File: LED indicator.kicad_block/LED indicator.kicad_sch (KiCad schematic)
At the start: 2 parts

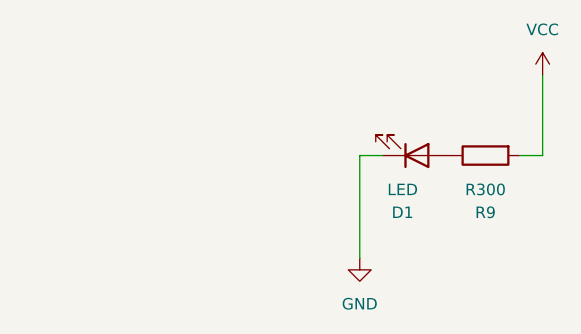
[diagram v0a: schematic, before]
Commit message: renamed indicator led block
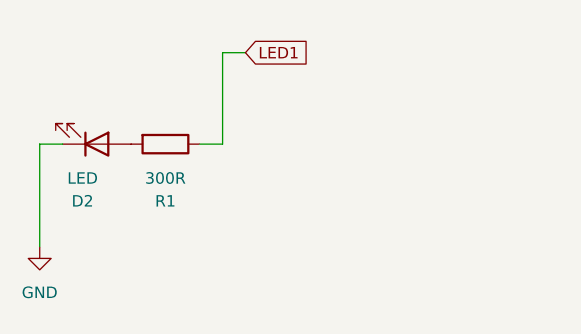
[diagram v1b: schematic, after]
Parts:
- removed D1: LED, LED_THT:LED_D5.0mm, symbol Device:LED
- removed R9: R300, symbol Device:R
- added D2: LED, LED_THT:LED_D5.0mm, symbol Device:LED
- added R1: 300R, symbol Device:R
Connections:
- net GND: now also D2.1 (K)
- new net: D2.2 (A), R1.2
- new net LED1: R1.1
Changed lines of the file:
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@@
 	(wire
 		(pts
-			(xy 274.32 93.98) (xy 271.78 93.98)
-		)
-		(stroke
-			(width 0)
-			(type default)
-		)
-	)
-	(wire
-		(pts
-			(xy 254 93.98) (xy 254 105.41)
-		)
-		(stroke
-			(width 0)
-			(type default)
-		)
-	)
-	(wire
-		(pts
-			(xy 256.54 93.98) (xy 254 93.98)
-		)
-		(stroke
-			(width 0)
-			(type default)
-		)
-	)
-	(wire
-		(pts
-			(xy 274.32 85.09) (xy 274.32 93.98)
-		)
-		(stroke
-			(width 0)
-			(type default)
+			(xy 238.76 92.71) (xy 236.22 92.71)
+		)
+		(stroke
+			(width 0)
+			(type default)
+		)
+	)
+	(wire
+		(pts
+			(xy 238.76 82.55) (xy 238.76 92.71)
+		)
+		(stroke
+			(width 0)
+			(type default)
+		)
+	)
+	(wire
+		(pts
+			(xy 241.3 82.55) (xy 238.76 82.55)
+		)
+		(stroke
+			(width 0)
+			(type default)
+		)
+	)
+	(wire
+		(pts
+			(xy 220.98 92.71) (xy 218.44 92.71)
+		)
+		(stroke
+			(width 0)
+			(type default)
+		)
+	)
+	(wire
+		(pts
+			(xy 218.44 92.71) (xy 218.44 104.14)
+		)
+		(stroke
+			(width 0)
+			(type default)
+		)
+	)
+	(global_label "LED1"
+		(shape input)
+		(at 241.3 82.55 0)
+		(fields_autoplaced yes)
+		(effects
+			(font
+				(size 1.27 1.27)
+			)
+			(justify left)
+		)
+		(property "Intersheetrefs" "${INTERSHEET_REFS}"
+			(at 248.9418 82.55 0)
+			(hide yes)
+			(show_name no)
+			(do_not_autoplace no)
+			(effects
+				(font
+					(size 1.27 1.27)
+				)
+				(justify left)
+			)
 		)
 	)
 	(symbol
 		(lib_id "Device:LED")
-		(at 260.35 93.98 0)
+		(at 224.79 92.71 0)
 		(mirror x)
 		(unit 1)
@@
 		(in_pos_files yes)
 		(dnp no)
-		(property "Reference" "D1"
-			(at 258.7625 100.33 0)
+		(property "Reference" "D2"
+			(at 223.2025 99.06 0)
 			(show_name no)
 			(do_not_autoplace no)
@@
 		)
 		(property "Value" "LED"
-			(at 258.7625 97.79 0)
+			(at 223.2025 96.52 0)
 			(show_name no)
 			(do_not_autoplace no)
@@
 		)
 		(property "Footprint" "LED_THT:LED_D5.0mm"
-			(at 260.35 93.98 0)
+			(at 224.79 92.71 0)
 			(hide yes)
 			(show_name no)
@@
 		)
 		(property "Datasheet" ""
-			(at 260.35 93.98 0)
+			(at 224.79 92.71 0)
 			(hide yes)
 			(show_name no)
@@
 		)
 		(property "Description" "Light emitting diode"
-			(at 260.35 93.98 0)
+			(at 224.79 92.71 0)
 			(hide yes)
 			(show_name no)
@@
 		)
 		(property "Sim.Pins" "1=K 2=A"
-			(at 260.35 93.98 0)
+			(at 224.79 92.71 0)
 			(hide yes)
 			(show_name no)
@@
 		)
 		(instances
-			(project "MobiFlight-kicad-blocks-source"
+			(project "kicad-mobiflight-device-blocks-worksheet"
 				(path "/4714e232-3dfb-45f4-a0c3-3539b78f5138"
-					(reference "D1")
+					(reference "D2")
 					(unit 1)
 				)
@@
 	)
 	(symbol
-		(lib_id "power:VCC")
-		(at 274.32 85.09 0)
+		(lib_id "Device:R")
+		(at 232.41 92.71 270)
+		(unit 1)
+		(body_style 1)
+		(exclude_from_sim no)
+		(in_bom yes)
+		(on_board yes)
+		(in_pos_files yes)
+		(dnp no)
+		(property "Reference" "R1"
+			(at 232.41 99.06 90)
+			(show_name no)
+			(do_not_autoplace no)
+			(effects
+				(font
+					(size 1.27 1.27)
+				)
+			)
+		)
+		(property "Value" "300R"
+			(at 232.41 96.52 90)
+			(show_name no)
+			(do_not_autoplace no)
+			(effects
+				(font
+					(size 1.27 1.27)
+				)
+			)
+		)
+		(property "Footprint" ""
+			(at 232.41 90.932 90)
+			(hide yes)
+			(show_name no)
+			(do_not_autoplace no)
+			(effects
+				(font
+					(size 1.27 1.27)
+				)
+			)
+		)
+		(property "Datasheet" ""
+			(at 232.41 92.71 0)
+			(hide yes)
+			(show_name no)
+			(do_not_autoplace no)
+			(effects
+				(font
+					(size 1.27 1.27)
+				)
+			)
+		)
+		(property "Description" "Resistor"
+			(at 232.41 92.71 0)
+			(hide yes)
+			(show_name no)
+			(do_not_autoplace no)
+			(effects
+				(font
+					(size 1.27 1.27)
+				)
+			)
+		)
+		(pin "1"
+		)
+		(pin "2"
+		)
+		(instances
+			(project "kicad-mobiflight-device-blocks-worksheet"
+				(path "/4714e232-3dfb-45f4-a0c3-3539b78f5138"
+					(reference "R1")
+					(unit 1)
+				)
+			)
+		)
+	)
+	(symbol
+		(lib_id "power:GND")
+		(at 218.44 104.14 0)
 		(unit 1)
 		(body_style 1)
@@
 		(dnp no)
 		(fields_autoplaced yes)
-		(property "Reference" "#PWR012"
-			(at 274.32 88.9 0)
-			(hide yes)
-			(show_name no)
-			(do_not_autoplace no)
-			(effects
-				(font
-					(size 1.27 1.27)
-				)
-			)
-		)
-		(property "Value" "VCC"
-			(at 274.32 80.01 0)
+		(property "Reference" "#PWR015"
+			(at 218.44 110.49 0)
+			(hide yes)
+			(show_name no)
+			(do_not_autoplace no)
+			(effects
+				(font
+					(size 1.27 1.27)
+				)
+			)
+		)
+		(property "Value" "GND"
+			(at 218.44 109.22 0)
 			(show_name no)
 			(do_not_autoplace no)
@@
 		)
 		(property "Footprint" ""
-			(at 274.32 85.09 0)
+			(at 218.44 104.14 0)
 			(hide yes)
 			(show_name no)
@@
 		)
 		(property "Datasheet" ""
-			(at 274.32 85.09 0)
-			(hide yes)
-			(show_name no)
-			(do_not_autoplace no)
-			(effects
-				(font
-					(size 1.27 1.27)
-				)
-			)
-		)
-		(property "Description" "Power symbol creates a global label with name \"VCC\""
-			(at 274.32 85.09 0)
+			(at 218.44 104.14 0)
+			(hide yes)
+			(show_name no)
+			(do_not_autoplace no)
+			(effects
+				(font
+					(size 1.27 1.27)
+				)
+			)
+		)
+		(property "Description" "Power symbol creates a global label with name \"GND\" , ground"
+			(at 218.44 104.14 0)
 			(hide yes)
 			(show_name no)
@@
 		)
 		(instances
-			(project "MobiFlight-kicad-blocks-source"
+			(project "kicad-mobiflight-device-blocks-worksheet"
 				(path "/4714e232-3dfb-45f4-a0c3-3539b78f5138"
-					(reference "#PWR012")
+					(reference "#PWR015")
 					(unit 1)
 				)
-			)
-		)
-	)
-	(symbol
-		(lib_id "power:GND")
-		(at 254 105.41 0)
-		(unit 1)
-		(body_style 1)
-		(exclude_from_sim no)
-		(in_bom yes)
-		(on_board yes)
-		(in_pos_files yes)
-		(dnp no)
-		(fields_autoplaced yes)
-		(property "Reference" "#PWR011"
-			(at 254 111.76 0)
-			(hide yes)
-			(show_name no)
-			(do_not_autoplace no)
-			(effects
-				(font
-					(size 1.27 1.27)
-				)
-			)
-		)
-		(property "Value" "GND"
-			(at 254 110.49 0)
-			(show_name no)
-			(do_not_autoplace no)
-			(effects
-				(font
-					(size 1.27 1.27)
-				)
-			)
-		)
-		(property "Footprint" ""
-			(at 254 105.41 0)
-			(hide yes)
-			(show_name no)
-			(do_not_autoplace no)
-			(effects
-				(font
-					(size 1.27 1.27)
-				)
-			)
-		)
-		(property "Datasheet" ""
-			(at 254 105.41 0)
-			(hide yes)
-			(show_name no)
-			(do_not_autoplace no)
-			(effects
-				(font
-					(size 1.27 1.27)
-				)
-			)
-		)
-		(property "Description" "Power symbol creates a global label with name \"GND\" , ground"
-			(at 254 105.41 0)
-			(hide yes)
-			(show_name no)
-			(do_not_autoplace no)
-			(effects
-				(font
-					(size 1.27 1.27)
-				)
-			)
-		)
-		(pin "1"
-		)
-		(instances
-			(project "MobiFlight-kicad-blocks-source"
-				(path "/4714e232-3dfb-45f4-a0c3-3539b78f5138"
-					(reference "#PWR011")
-					(unit 1)
-				)
-			)
-		)
-	)
-	(symbol
-		(lib_id "Device:R")
-		(at 267.97 93.98 90)
-		(mirror x)
-		(unit 1)
-		(body_style 1)
-		(exclude_from_sim no)
-		(in_bom yes)
-		(on_board yes)
-		(in_pos_files yes)
-		(dnp no)
-		(property "Reference" "R9"
-			(at 267.97 100.33 90)
-			(show_name no)
-			(do_not_autoplace no)
-			(effects
-				(font
-					(size 1.27 1.27)
-				)
-			)
-		)
-		(property "Value" "R300"
-			(at 267.97 97.79 90)
-			(show_name no)
-			(do_not_autoplace no)
-			(effects
-				(font
-					(size 1.27 1.27)
-				)
-			)
-		)
-		(property "Footprint" ""
-			(at 267.97 92.202 90)
-			(hide yes)
-			(show_name no)
-			(do_not_autoplace no)
-			(effects
-				(font
-					(size 1.27 1.27)
-				)
-			)
-		)
-		(property "Datasheet" ""
-			(at 267.97 93.98 0)
-			(hide yes)
-			(show_name no)
-			(do_not_autoplace no)
-			(effects
-				(font
-					(size 1.27 1.27)
-				)
-			)
-		)
-		(property "Description" "Resistor"
-			(at 267.97 93.98 0)
-			(hide yes)
-			(show_name no)
-			(do_not_autoplace no)
-			(effects
-				(font
-					(size 1.27 1.27)
-				)
-			)
-		)
-		(pin "1"
-		)
-		(pin "2"
-		)
-		(instances
-			(project "MobiFlight-kicad-blocks-source"
-				(path "/4714e232-3dfb-45f4-a0c3-3539b78f5138"
-					(reference "R9")
-					(unit 1)
-				)
